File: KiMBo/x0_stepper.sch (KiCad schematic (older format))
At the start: 25 parts, among them U19 TMC2130

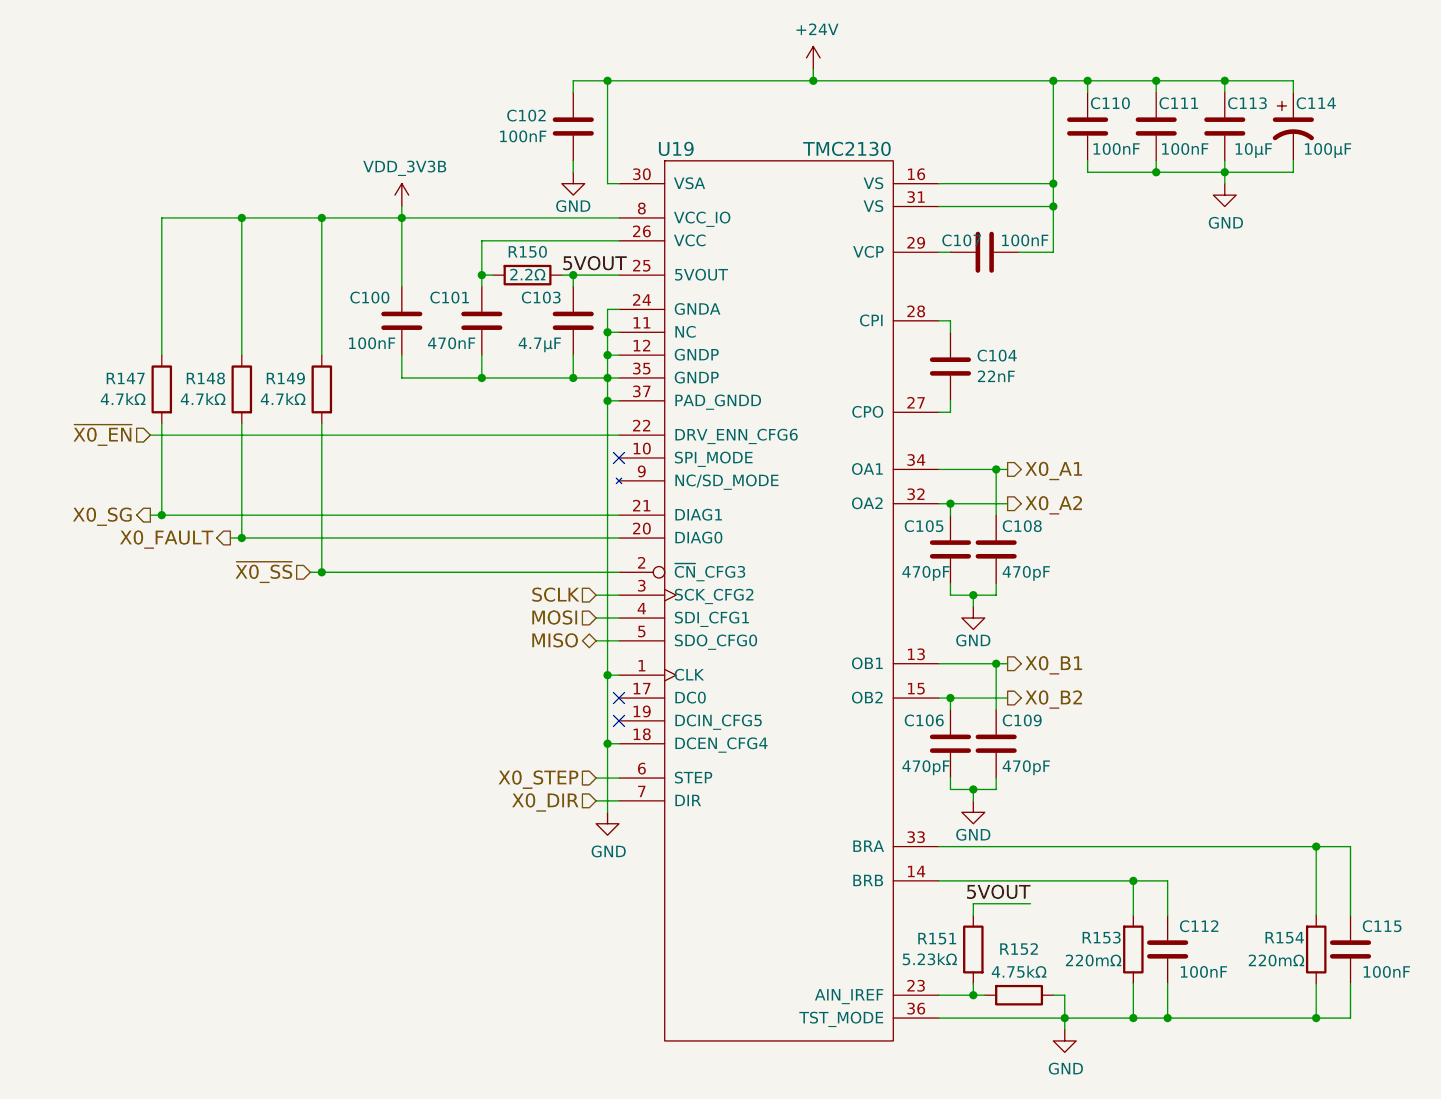
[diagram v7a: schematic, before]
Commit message: Remove HDMI from the schematic
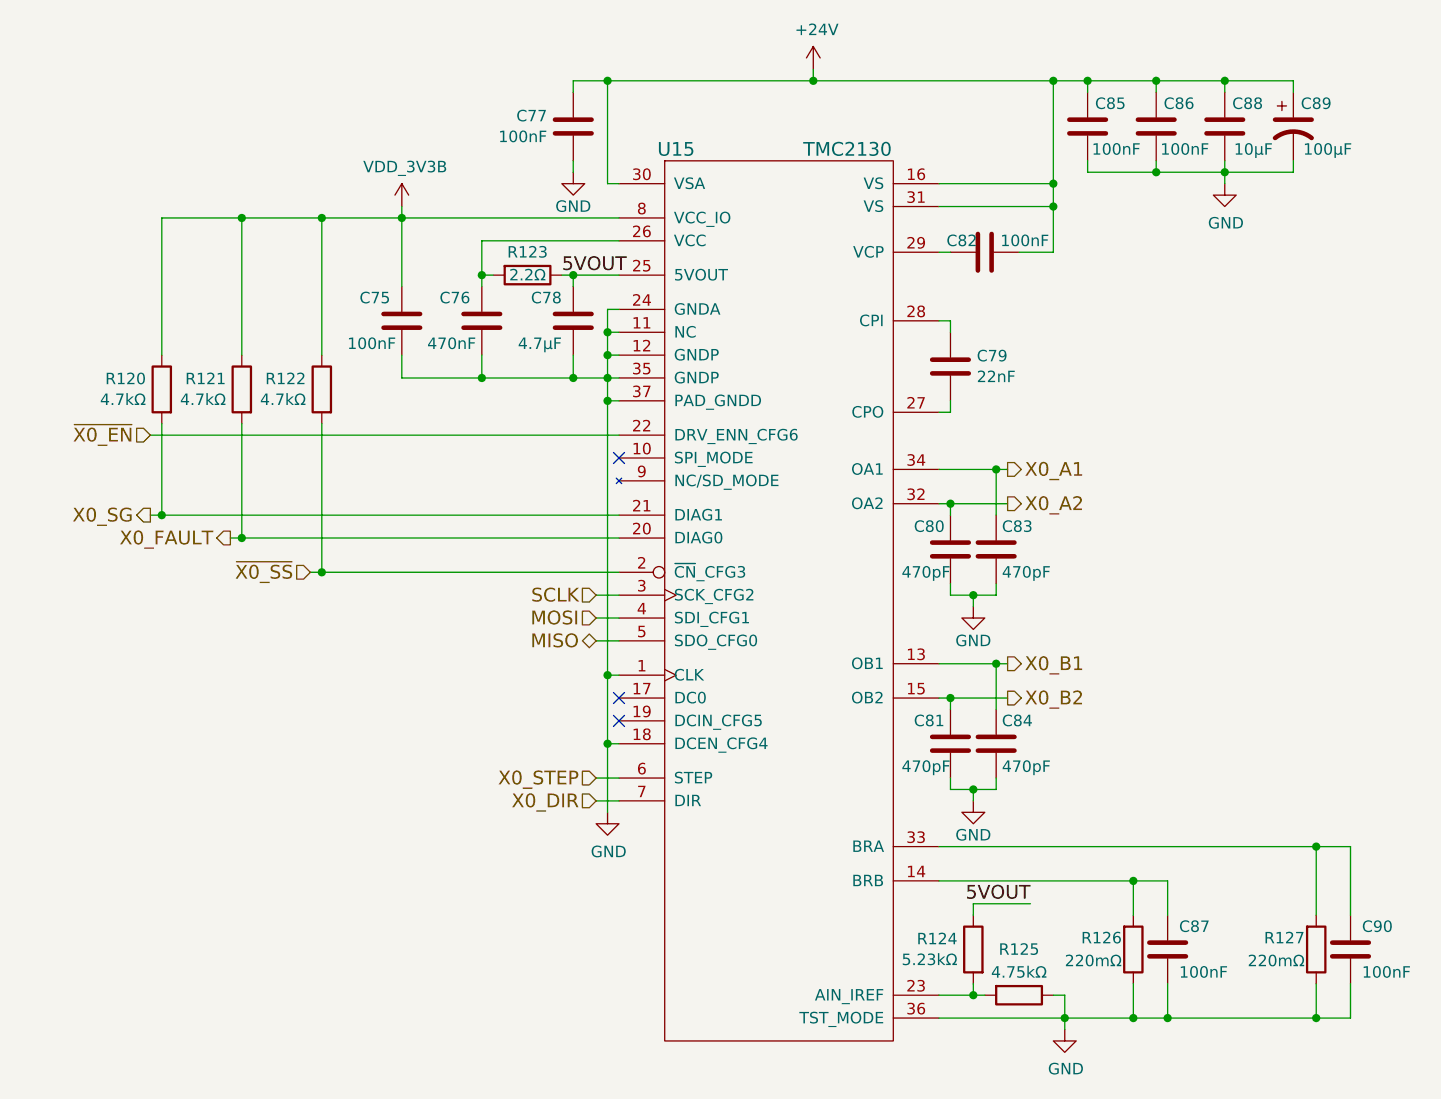
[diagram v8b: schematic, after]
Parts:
- renumbered C100 to C75, C101 to C76, C102 to C77, C103 to C78, C104 to C79, C105 to C80, C106 to C81, C107 to C82, C108 to C83, C109 to C84, C110 to C85, C111 to C86, C112 to C87, C113 to C88, C114 to C89, C115 to C90, R147 to R120, R148 to R121, R149 to R122, R150 to R123, R151 to R124, R152 to R125, R153 to R126, R154 to R127, U19 to U15
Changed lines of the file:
@@
 $Descr A3 16535 11693
 encoding utf-8
-Sheet 17 26
+Sheet 17 25
 Title ""
 Date ""
@@
 X0_SG
 $Comp
-L C C102
+L C C77
 U 1 1 5BA7E13B
 P 7500 3100
-F 0 "C102" H 7386 3054 50  0000 R CNN
+F 0 "C77" H 7386 3054 50  0000 R CNN
 F 1 "100nF" H 7386 3145 50  0000 R CNN
 F 2 "Capacitors_SMD:C_0603" H 7538 2950 50  0001 C CNN
@@
 $EndComp
 $Comp
-L C C107
+L C C82
 U 1 1 5BA7E13C
 P 9300 3650
-F 0 "C107" V 9250 3550 50  0000 C CNN
+F 0 "C82" V 9250 3550 50  0000 C CNN
 F 1 "100nF" V 9250 3825 50  0000 C CNN
 F 2 "Capacitors_SMD:C_0603" H 9338 3500 50  0001 C CNN
@@
 $EndComp
 $Comp
-L CP1 C114
+L CP1 C89
 U 1 1 58C092C4
 P 10650 3100
-F 0 "C114" H 10750 3200 50  0000 C CNN
+F 0 "C89" H 10750 3200 50  0000 C CNN
 F 1 "100μF" H 10800 3000 50  0000 C CNN
 F 2 "Capacitors_SMD:c_elec_8x10" H 10650 3100 50  0001 C CNN
@@
 $EndComp
 $Comp
-L C C110
+L C C85
 U 1 1 58C092CB
 P 9750 3100
-F 0 "C110" H 9650 3200 50  0000 C CNN
+F 0 "C85" H 9650 3200 50  0000 C CNN
 F 1 "100nF" H 9625 3000 50  0000 C CNN
 F 2 "Capacitors_SMD:C_0603" H 9788 2950 50  0001 C CNN
@@
 $EndComp
 $Comp
-L GND #PWR0208
+L GND #PWR0177
 U 1 1 58C092D2
 P 7500 3300
-F 0 "#PWR0208" H 7500 3050 50  0001 C CNN
+F 0 "#PWR0177" H 7500 3050 50  0001 C CNN
 F 1 "GND" H 7500 3150 50  0000 C CNN
 F 2 "" H 7500 3300 50  0000 C CNN
@@
 $EndComp
 $Comp
-L C C111
+L C C86
 U 1 1 5BA7E140
 P 10050 3100
-F 0 "C111" H 9950 3200 50  0000 C CNN
+F 0 "C86" H 9950 3200 50  0000 C CNN
 F 1 "100nF" H 9925 3000 50  0000 C CNN
 F 2 "Capacitors_SMD:C_0603" H 10088 2950 50  0001 C CNN
@@
 $EndComp
 $Comp
-L GND #PWR0209
+L GND #PWR0178
 U 1 1 5BA7E141
 P 10350 3350
-F 0 "#PWR0209" H 10350 3100 50  0001 C CNN
+F 0 "#PWR0178" H 10350 3100 50  0001 C CNN
 F 1 "GND" H 10355 3177 50  0000 C CNN
 F 2 "" H 10350 3350 50  0000 C CNN
@@
 $EndComp
 $Comp
-L +24V #PWR0210
+L +24V #PWR0179
 U 1 1 58C092E5
 P 8550 2850
-F 0 "#PWR0210" H 8550 2700 50  0001 C CNN
+F 0 "#PWR0179" H 8550 2700 50  0001 C CNN
 F 1 "+24V" H 8565 3023 50  0000 C CNN
 F 2 "" H 8550 2850 50  0000 C CNN
@@
 $EndComp
 $Comp
-L C C104
+L C C79
 U 1 1 58C092EB
 P 9150 4150
-F 0 "C104" H 9265 4196 50  0000 L CNN
+F 0 "C79" H 9265 4196 50  0000 L CNN
 F 1 "22nF" H 9265 4105 50  0000 L CNN
 F 2 "Capacitors_SMD:C_0603" H 9188 4000 50  0001 C CNN
@@
 $EndComp
 $Comp
-L R R154
+L R R127
 U 1 1 58C092F2
 P 10750 6700
-F 0 "R154" H 10700 6650 50  0000 R CNN
+F 0 "R127" H 10700 6650 50  0000 R CNN
 F 1 "220mΩ" H 10700 6750 50  0000 R CNN
 F 2 "Resistors_SMD:R_0805" V 10680 6700 50  0001 C CNN
@@
 $EndComp
 $Comp
-L R R153
+L R R126
 U 1 1 58C092F9
 P 9950 6700
-F 0 "R153" H 9900 6650 50  0000 R CNN
+F 0 "R126" H 9900 6650 50  0000 R CNN
 F 1 "220mΩ" H 9900 6750 50  0000 R CNN
 F 2 "Resistors_SMD:R_0805" V 9880 6700 50  0001 C CNN
@@
 $EndComp
 $Comp
-L GND #PWR0211
+L GND #PWR0180
 U 1 1 5BA7E146
 P 9650 7050
-F 0 "#PWR0211" H 9650 6800 50  0001 C CNN
+F 0 "#PWR0180" H 9650 6800 50  0001 C CNN
 F 1 "GND" H 9655 6877 50  0000 C CNN
 F 2 "" H 9650 7050 50  0000 C CNN
@@
 NoConn ~ 7700 5600
 $Comp
-L R R150
+L R R123
 U 1 1 5BA7E147
 P 7300 3750
-F 0 "R150" V 7200 3750 50  0000 C CNN
+F 0 "R123" V 7200 3750 50  0000 C CNN
 F 1 "2.2Ω" V 7300 3750 50  0000 C CNN
 F 2 "Resistors_SMD:R_0603" V 7230 3750 50  0001 C CNN
@@
 $EndComp
 $Comp
-L C C101
+L C C76
 U 1 1 5BA7E148
 P 7100 3950
-F 0 "C101" H 7150 4050 50  0000 L CNN
+F 0 "C76" H 7150 4050 50  0000 L CNN
 F 1 "470nF" H 7125 3850 50  0000 L CNN
 F 2 "Capacitors_SMD:C_0603" H 7138 3800 50  0001 C CNN
@@
 NoConn ~ 7700 5700
 $Comp
-L GND #PWR0212
+L GND #PWR0181
 U 1 1 5BA7E149
 P 7650 6100
-F 0 "#PWR0212" H 7650 5850 50  0001 C CNN
+F 0 "#PWR0181" H 7650 5850 50  0001 C CNN
 F 1 "GND" H 7655 5927 50  0000 C CNN
 F 2 "" H 7650 6100 50  0000 C CNN
@@
 $EndComp
 $Comp
-L C C112
+L C C87
 U 1 1 5BA7E14A
 P 10100 6700
-F 0 "C112" H 10150 6800 50  0000 L CNN
+F 0 "C87" H 10150 6800 50  0000 L CNN
 F 1 "100nF" H 10150 6600 50  0000 L CNN
 F 2 "Capacitors_SMD:C_0603" H 10138 6550 50  0001 C CNN
@@
 X0_FAULT
 $Comp
-L R R148
+L R R121
 U 1 1 58C09331
 P 6050 4250
-F 0 "R148" H 6119 4296 50  0000 L CNN
+F 0 "R121" H 6119 4296 50  0000 L CNN
 F 1 "4.7kΩ" H 6119 4205 50  0000 L CNN
 F 2 "Resistors_SMD:R_0603" V 5980 4250 50  0001 C CNN
@@
 NoConn ~ 7700 4550
 $Comp
-L C C103
+L C C78
 U 1 1 5BA7E14C
 P 7500 3950
-F 0 "C103" H 7550 4050 50  0000 L CNN
+F 0 "C78" H 7550 4050 50  0000 L CNN
 F 1 "4.7μF" H 7550 3850 50  0000 L CNN
 F 2 "Capacitors_SMD:C_0603" H 7538 3800 50  0001 C CNN
@@
 5VOUT
 $Comp
-L R R151
+L R R124
 U 1 1 5BA7E14D
 P 9250 6700
-F 0 "R151" H 9319 6746 50  0000 L CNN
+F 0 "R124" H 9319 6746 50  0000 L CNN
 F 1 "5.23kΩ" H 9319 6655 50  0000 L CNN
 F 2 "Resistors_SMD:R_0603" V 9180 6700 50  0001 C CNN
@@
 5VOUT
 $Comp
-L R R152
+L R R125
 U 1 1 5BA7E14E
 P 9450 6900
-F 0 "R152" V 9250 6900 50  0000 C CNN
+F 0 "R125" V 9250 6900 50  0000 C CNN
 F 1 "4.75kΩ" V 9350 6900 50  0000 C CNN
 F 2 "Resistors_SMD:R_0603" V 9380 6900 50  0001 C CNN
@@
 $EndComp
 $Comp
-L R R149
+L R R122
 U 1 1 58C09353
 P 6400 4250
-F 0 "R149" H 6469 4296 50  0000 L CNN
+F 0 "R122" H 6469 4296 50  0000 L CNN
 F 1 "4.7kΩ" H 6469 4205 50  0000 L CNN
 F 2 "Resistors_SMD:R_0603" V 6330 4250 50  0001 C CNN
@@
 $EndComp
 $Comp
-L C C115
+L C C90
 U 1 1 58C0935A
 P 10900 6700
-F 0 "C115" H 10950 6800 50  0000 L CNN
+F 0 "C90" H 10950 6800 50  0000 L CNN
 F 1 "100nF" H 10950 6600 50  0000 L CNN
 F 2 "Capacitors_SMD:C_0603" H 10938 6550 50  0001 C CNN
@@
 $EndComp
 $Comp
-L C C105
+L C C80
 U 1 1 58C09363
 P 9150 4950
-F 0 "C105" H 9175 5050 50  0000 L CNN
+F 0 "C80" H 9175 5050 50  0000 L CNN
 F 1 "470pF" H 9150 4850 50  0000 L CNN
 F 2 "Capacitors_SMD:C_0603" H 9188 4800 50  0001 C CNN
@@
 $EndComp
 $Comp
-L GND #PWR0213
+L GND #PWR0182
 U 1 1 58C0936A
 P 9250 5200
-F 0 "#PWR0213" H 9250 4950 50  0001 C CNN
+F 0 "#PWR0182" H 9250 4950 50  0001 C CNN
 F 1 "GND" H 9250 5050 50  0000 C CNN
 F 2 "" H 9250 5200 50  0000 C CNN
@@
 $EndComp
 $Comp
-L C C108
+L C C83
 U 1 1 58C09370
 P 9350 4950
-F 0 "C108" H 9375 5050 50  0000 L CNN
+F 0 "C83" H 9375 5050 50  0000 L CNN
 F 1 "470pF" H 9375 4850 50  0000 L CNN
 F 2 "Capacitors_SMD:C_0603" H 9388 4800 50  0001 C CNN
@@
 $EndComp
 $Comp
-L C C106
+L C C81
 U 1 1 5BA7E154
 P 9150 5800
-F 0 "C106" H 9175 5900 50  0000 L CNN
+F 0 "C81" H 9175 5900 50  0000 L CNN
 F 1 "470pF" H 9150 5700 50  0000 L CNN
 F 2 "Capacitors_SMD:C_0603" H 9188 5650 50  0001 C CNN
@@
 $EndComp
 $Comp
-L GND #PWR0214
+L GND #PWR0183
 U 1 1 58C0937E
 P 9250 6050
-F 0 "#PWR0214" H 9250 5800 50  0001 C CNN
+F 0 "#PWR0183" H 9250 5800 50  0001 C CNN
 F 1 "GND" H 9250 5900 50  0000 C CNN
 F 2 "" H 9250 6050 50  0000 C CNN
@@
 $EndComp
 $Comp
-L C C109
+L C C84
 U 1 1 58C09384
 P 9350 5800
-F 0 "C109" H 9375 5900 50  0000 L CNN
+F 0 "C84" H 9375 5900 50  0000 L CNN
 F 1 "470pF" H 9375 5700 50  0000 L CNN
 F 2 "Capacitors_SMD:C_0603" H 9388 5650 50  0001 C CNN
@@
 $EndComp
 $Comp
-L TMC2130 U19
+L TMC2130 U15
 U 1 1 58C0938B
 P 8400 4700
-F 0 "U19" H 7950 6200 60  0000 C CNN
+F 0 "U15" H 7950 6200 60  0000 C CNN
 F 1 "TMC2130" H 8700 6200 60  0000 C CNN
 F 2 "KiMBo:QFN36_5X6" H 8400 5000 60  0001 C CNN
@@
 	9150 6000 9150 5950
 $Comp
-L R R147
+L R R120
 U 1 1 5BA7E158
 P 5700 4250
-F 0 "R147" H 5769 4296 50  0000 L CNN
+F 0 "R120" H 5769 4296 50  0000 L CNN
 F 1 "4.7kΩ" H 5769 4205 50  0000 L CNN
 F 2 "Resistors_SMD:R_0603" V 5630 4250 50  0001 C CNN
@@
 Connection ~ 6050 3500
 $Comp
-L C C113
+L C C88
 U 1 1 5BA7E159
 P 10350 3100
-F 0 "C113" H 10250 3200 50  0000 C CNN
+F 0 "C88" H 10250 3200 50  0000 C CNN
 F 1 "10μF" H 10225 3000 50  0000 C CNN
 F 2 "Capacitors_SMD:C_0805" H 10388 2950 50  0001 C CNN
@@
 	5700 3500 7700 3500
 $Comp
-L VDD_3V3B #PWR0215
+L VDD_3V3B #PWR0184
 U 1 1 5A2FF856
 P 6750 3450
-F 0 "#PWR0215" H 6750 3300 50  0001 C CNN
+F 0 "#PWR0184" H 6750 3300 50  0001 C CNN
 F 1 "VDD_3V3B" H 6765 3623 50  0000 C CNN
 F 2 "" H 6750 3450 50  0000 C CNN
@@
 $EndComp
 $Comp
-L C C100
+L C C75
 U 1 1 5A89853C
 P 6750 3950
-F 0 "C100" H 6800 4050 50  0000 L CNN
+F 0 "C75" H 6800 4050 50  0000 L CNN
 F 1 "100nF" H 6775 3850 50  0000 L CNN
 F 2 "Capacitors_SMD:C_0603" H 6788 3800 50  0001 C CNN
